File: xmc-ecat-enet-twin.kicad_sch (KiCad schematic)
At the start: 7 parts, among them U11 UMW3157, Y2 Oscillator_25M_3225_3v3_YSO11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

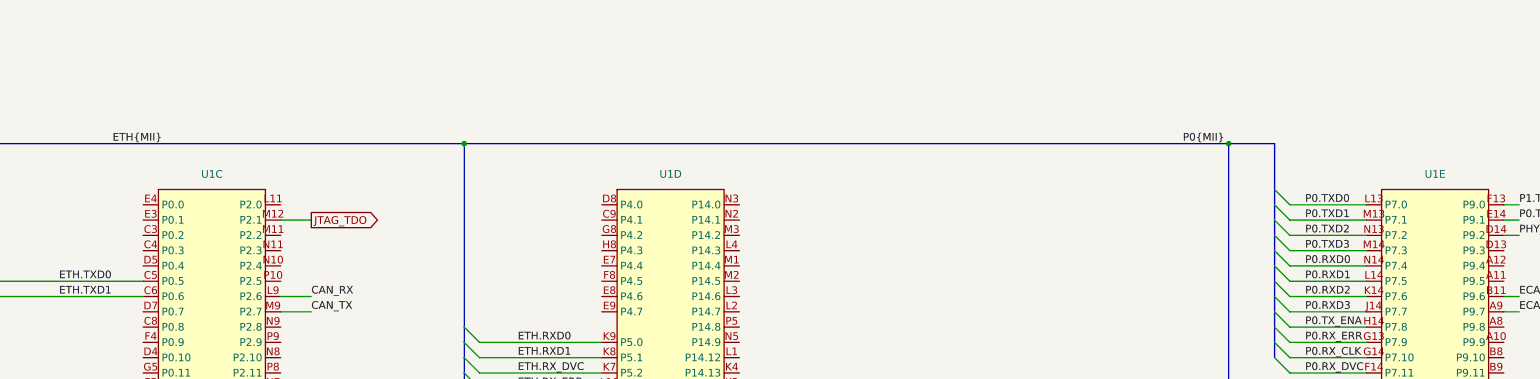
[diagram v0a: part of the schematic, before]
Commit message: finish a 24V supply
went with a more modern one, plenty of room.  Should be pretty good now.
Went over and filled in a bunch of missing parts and things, cleaned up
as much as I could 0603 vs 0402 for most, updated some thigns to current
atomic part library.

still to go, the "pi" interface and some sort of spi/io interface?
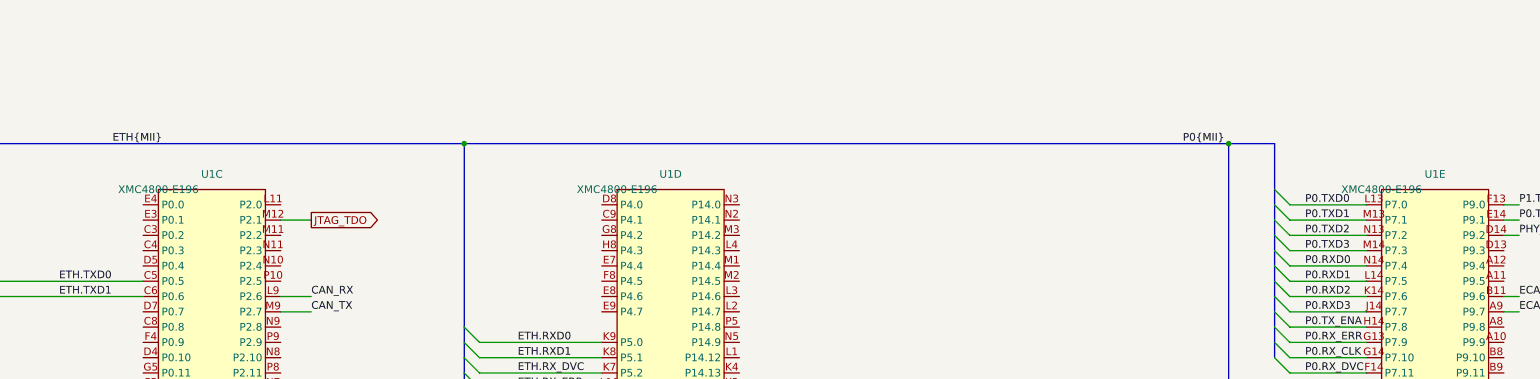
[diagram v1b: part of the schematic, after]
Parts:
- U1: value (none) -> XMC4800-E196

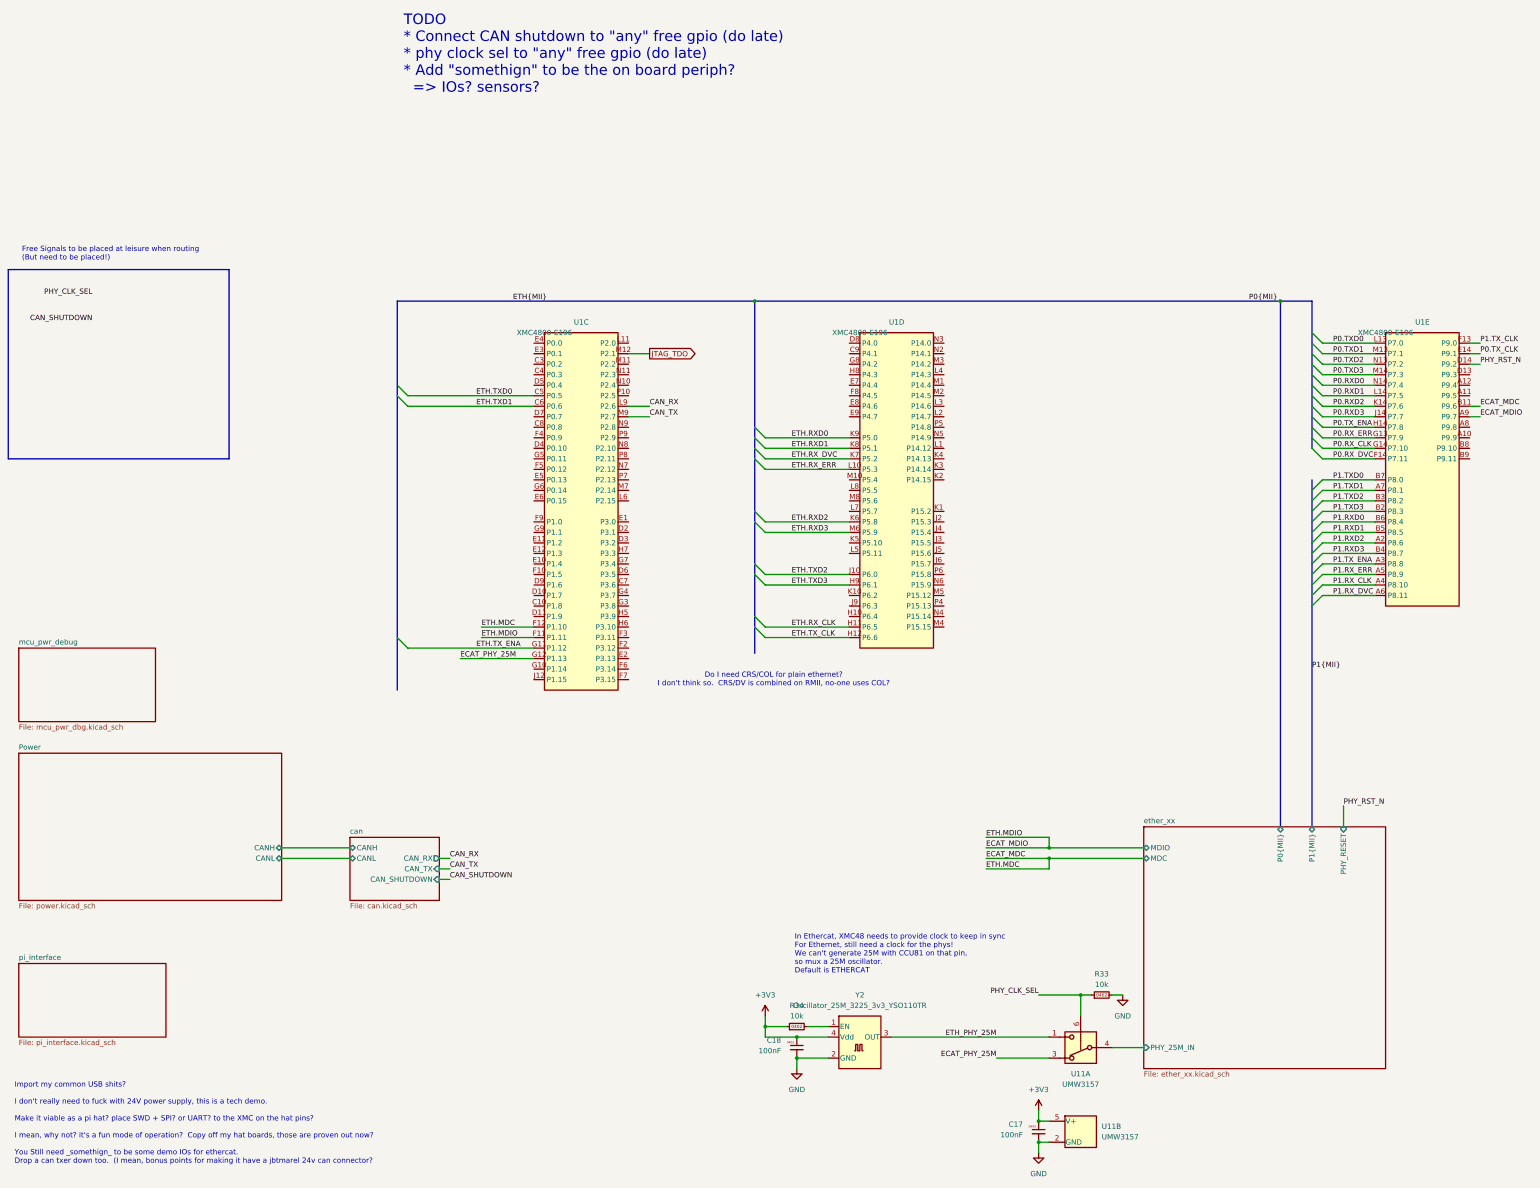
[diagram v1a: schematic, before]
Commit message: connect spi and uart to pi interface
we'll even have jumpers for being the hat or the baseboard for uart...

need to re-open modus to find new pins for i2c...
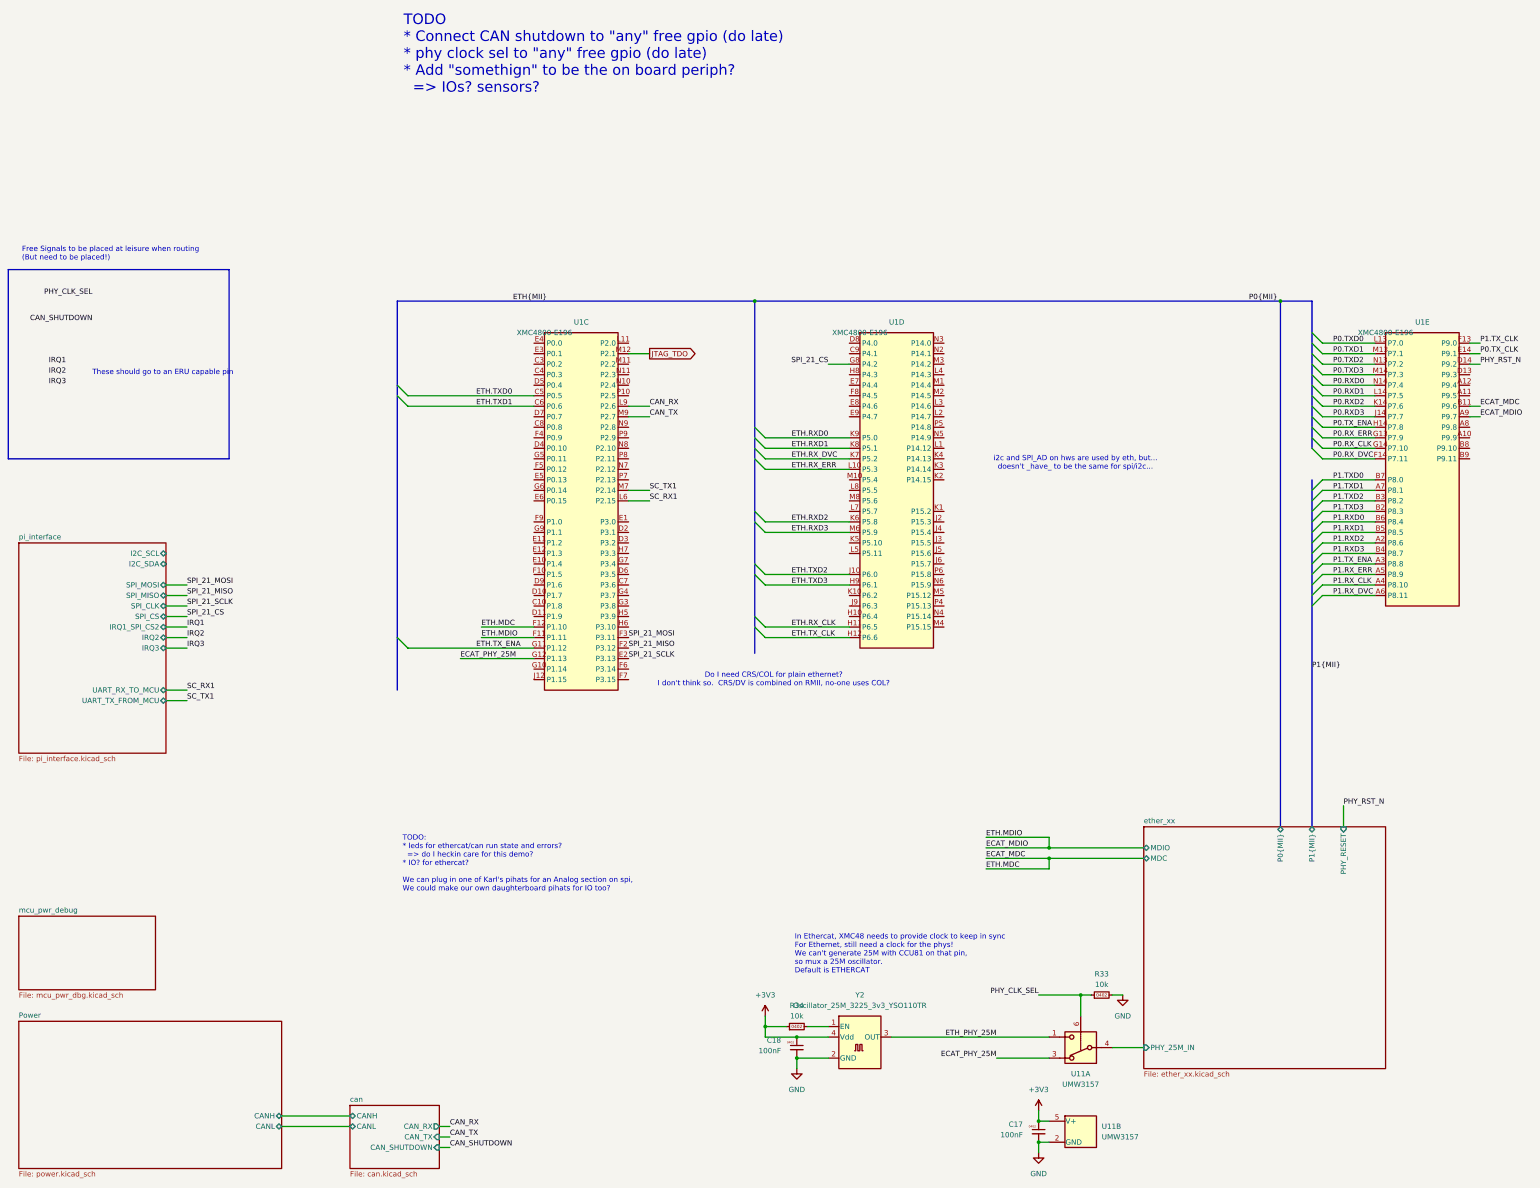
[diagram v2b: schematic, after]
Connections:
- net SPI_21_SCLK: now reaches U1.E2 (P3.13)
- net SPI_21_MISO: now reaches U1.F2 (P3.12)
- net SPI_21_MOSI: now reaches U1.F3 (P3.11)
- net SC_RX1: now reaches U1.L6 (P2.15)
- net SC_TX1: now reaches U1.M7 (P2.14)
- net SPI_21_CS: now reaches U1.G8 (P4.2)
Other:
- sheet pi_interface ports: added I2C_SCL, I2C_SDA, IRQ1_SPI_CS2, IRQ2, IRQ3, SPI_CLK, SPI_CS, SPI_MISO, SPI_MOSI, UART_RX_TO_MCU, UART_TX_FROM_MCU; removed none
- note added: "TODO: * leds for ethercat/can run state and errors? => do I heckin care for this demo? * IO? for ethercat? We can plug in one of Karl's pihats for an Analog section on spi, We could make our own daughterboard pihats for IO too?"
- note added: "These should go to an ERU capable pin"
- note added: "i2c and SPI_AD on hws are used by eth, but... doesn't _have_ to be the same for spi/i2c..."
- note removed: "Import my common USB shits? I don't really need to fuck with 24V power supply, this is a tech demo. Make it viable as a pi hat? place SWD + SPI? or UART? to the XMC on the hat pins? I mean, why not? it's a fun mode of operation? Copy off my hat boards, those are proven out now? You Still need _somethign_ to be some demo IOs for ethercat. Drop a can txer down too. (I mean, bonus points for making 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"

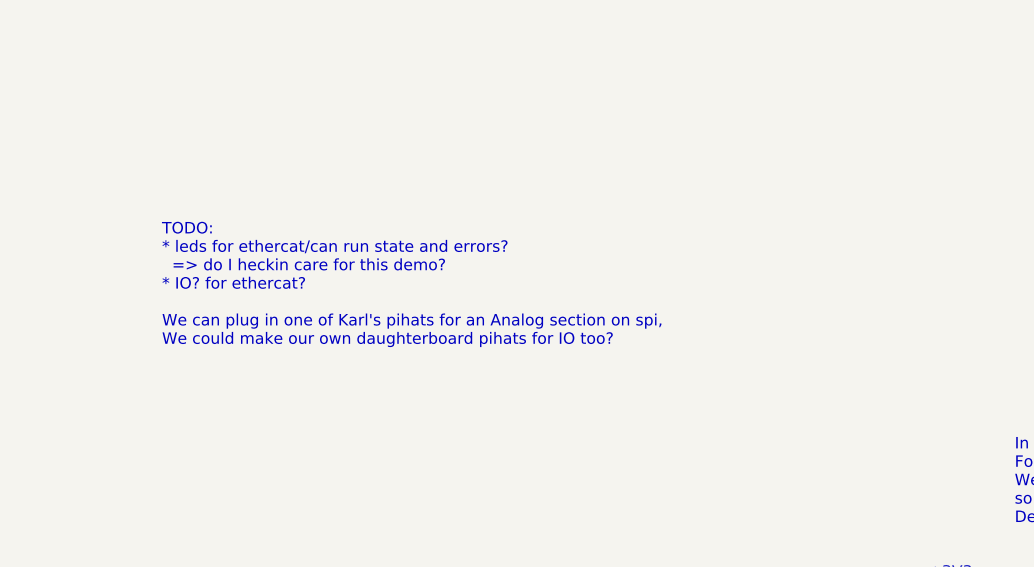
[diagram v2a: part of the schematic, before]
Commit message: start pcb?
already twisted to hell.  must be another choice for phy routing...
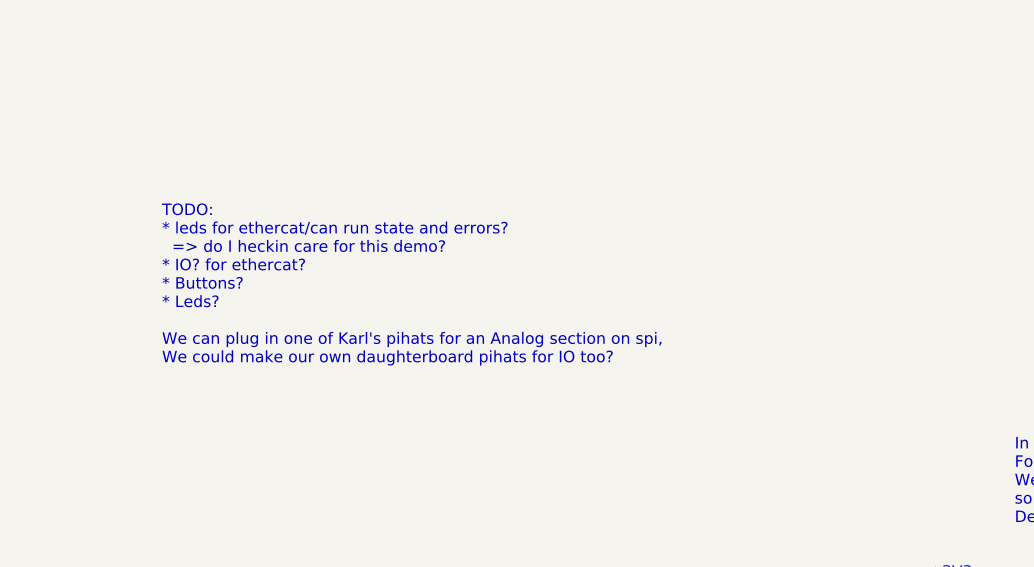
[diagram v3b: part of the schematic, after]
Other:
- note added: "TODO: * leds for ethercat/can run state and errors? => do I heckin care for this demo? * IO? for ethercat? * Buttons? * Leds? We can plug in one of Karl's pihats for an Analog section on spi, We could make our own daughterboard pihats for IO too?"
- note removed: "TODO: * leds for ethercat/can run state and errors? => do I heckin care for this demo? * IO? for ethercat? We can plug in one of Karl's pihats for an Analog section on spi, We could make our own daughterboard pihats for IO too?"
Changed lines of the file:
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@@
 		)
 	)
-	(text "TODO:\n* leds for ethercat/can run state and errors?\n  => do I heckin care for this demo?\n* IO? for ethercat?\n\nWe can plug in one of Karl's pihats for an Analog section on spi,\nWe could make our own daughterboard pihats for IO too?"
+	(text "TODO:\n* leds for ethercat/can run state and errors?\n  => do I heckin care for this demo?\n* IO? for ethercat?\n* Buttons?\n* Leds?\n\nWe can plug in one of Karl's pihats for an Analog section on spi,\nWe could make our own daughterboard pihats for IO too?"
 		(exclude_from_sim no)
 		(at 118.11 179.07 0)
